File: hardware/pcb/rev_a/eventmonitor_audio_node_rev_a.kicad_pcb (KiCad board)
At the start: 4 copper layers, 65 x 50 mm, 37 parts, among them J1 USB-C USB2.0, Q1 BC847B, Q2 BC847B, SW1 BOOT, SW2 RESET, U1 ESP32-S3-WROOM-1U-N16R8, U2 CP2102N-A02-GQFN24R, U3 AMS1117-3.3, U4 USBLC6-2SC6, U5 ICS-43434

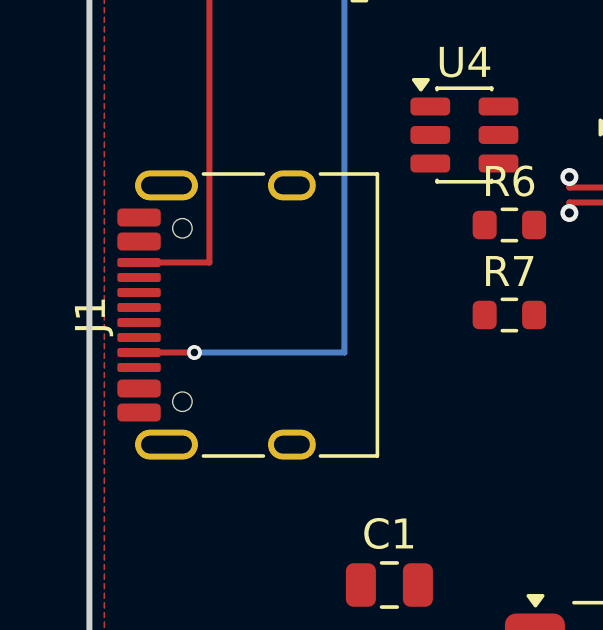
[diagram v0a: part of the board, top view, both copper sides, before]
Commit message: feat(pcb): connect Rev-A USB-C ground tabs
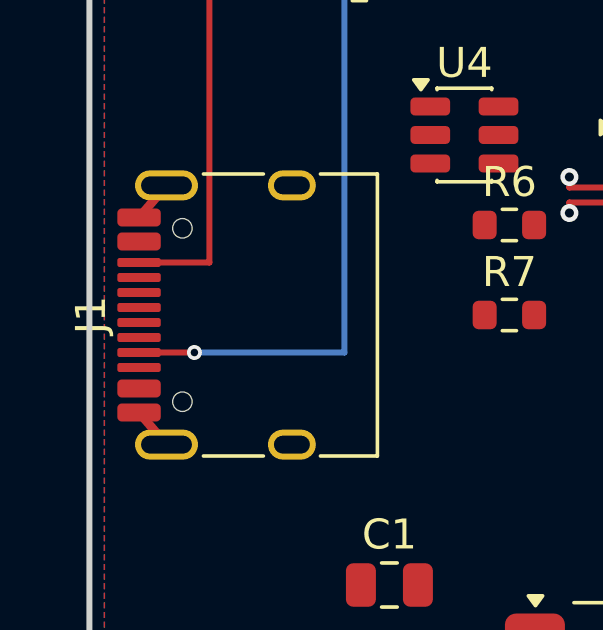
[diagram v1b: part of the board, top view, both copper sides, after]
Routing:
- net GND: track 0.00 -> 2.82 mm

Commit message: feat(pcb): complete Rev-A USB programming routing
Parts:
- moved U4 6.00 mm to (12.5, 25.0)
- moved R6 3.23 mm to (16.5, 24.1)
- moved R7 2.67 mm to (16.5, 25.9)
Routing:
- net EN: track 0.00 -> 60.0 mm, vias 0 -> 8
- net USB_5V: track 0.00 -> 50.6 mm, vias 0 -> 5
- net UART_TX_CP: track 0.00 -> 23.0 mm, vias 0 -> 2
- net USB_D-_ESD: track 0.00 -> 20.2 mm, vias 0 -> 3
- net USB_D+_ESD: track 0.00 -> 17.7 mm, vias 0 -> 3
- net UART_RX_CP: track 0.00 -> 13.5 mm, vias 0 -> 2
- net USB_CC1: track 26.4 -> 33.9 mm
- net +3V3: track 43.5 -> 50.8 mm, vias 13 -> 12
- net USB_D-: track 0.00 -> 7.30 mm, vias 0 -> 2
- net USB_D+: track 0.00 -> 6.88 mm, vias 0 -> 2
- net GND: track 2.82 -> 4.81 mm, vias 0 -> 2
- net AUTO_DTR: track 30.8 -> 30.1 mm
- net USB_CC2: track 15.8 -> 15.6 mm, vias 0 -> 2
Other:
- board text added: "REV-A / 4L / ROUTED"
- board text removed: "REV-A / 4L / POWER PLANES - UNROUTED"
